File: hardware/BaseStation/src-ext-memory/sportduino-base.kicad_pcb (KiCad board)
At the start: 2 copper layers, 76.8 x 45.7 mm, 43 parts, among them SW1 SW_Reed, X1 Battery, X2 Prog, X3 RC522

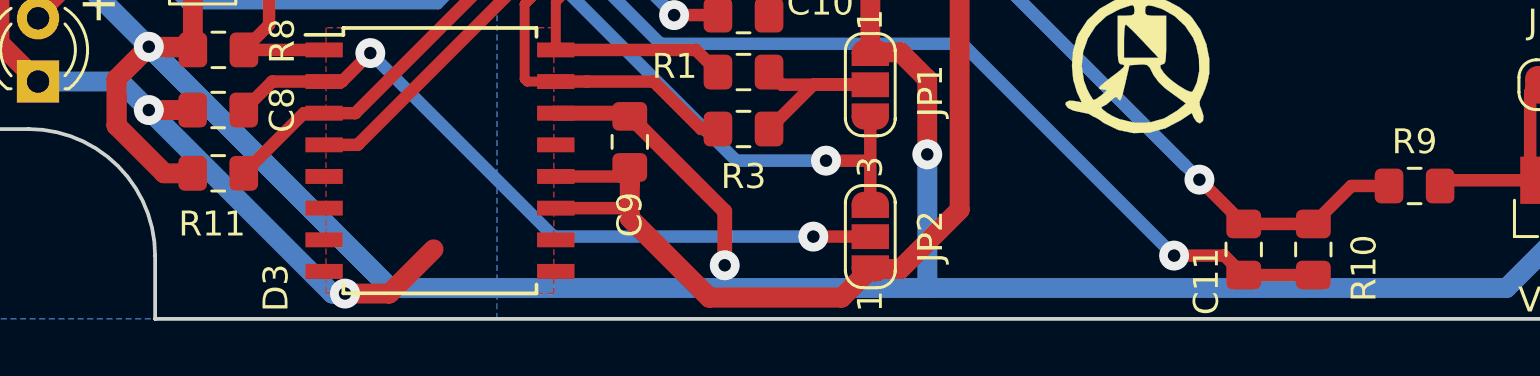
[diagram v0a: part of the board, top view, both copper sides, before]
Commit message: Base station PCB: updated assembly footprints positions
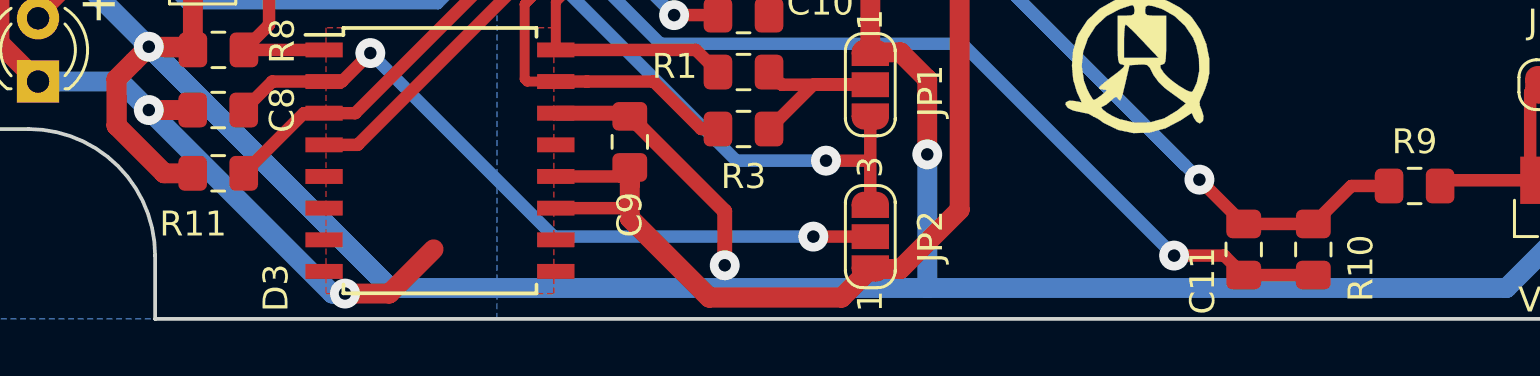
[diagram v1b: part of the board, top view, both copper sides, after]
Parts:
- ?: renamed from G***; value LOGO -> (none)
- BZ1: value TR1205Y -> (none)
- JP1, JP2: value SolderJumper_3_Bridged12 -> (none)
- JP3: value SolderJumper_2_Open -> (none)
- SW1: value SW_Reed -> (none)
- TP1, TP2, TP3, TP4, TP5: value TestPoint -> (none)
